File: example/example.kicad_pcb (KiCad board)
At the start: 2 copper layers, 43.2 x 35.6 mm, 12 parts, among them J1 Conn_01x07_Male, U1 LDC1314

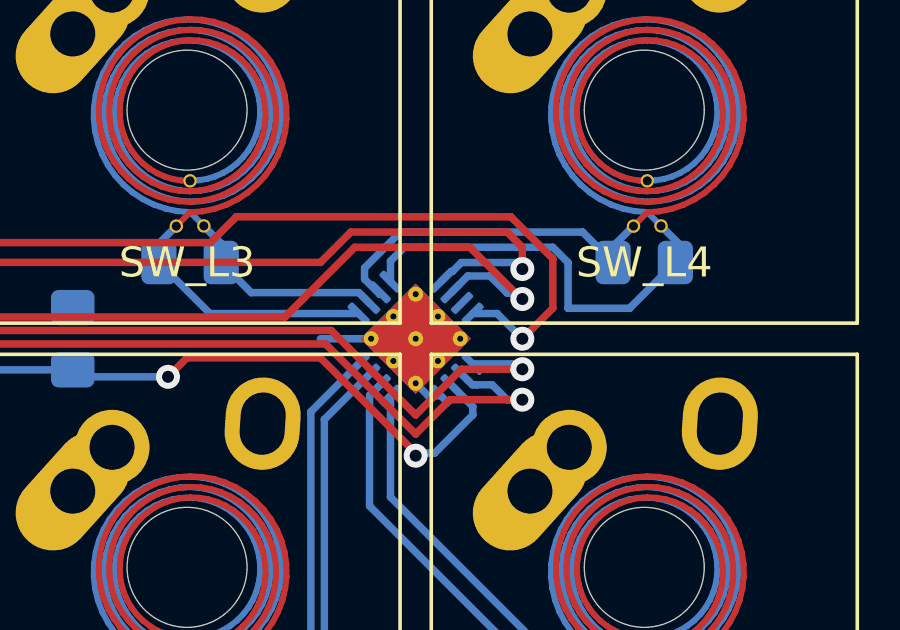
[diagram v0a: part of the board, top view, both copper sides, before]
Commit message: kikit for automatic fab output of example
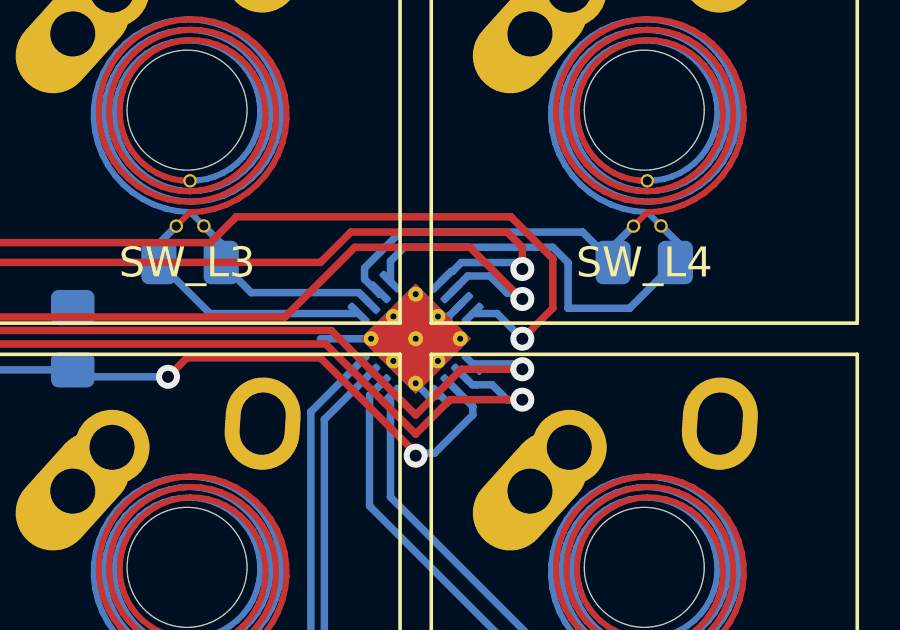
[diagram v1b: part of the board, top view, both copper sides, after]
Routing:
- net GND: track 2.70 -> 4.05 mm
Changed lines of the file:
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@@
   (segment (start 111.76 63.5) (end 111.76 65.024) (width 0.25) (layer "B.Cu") (net 8))
   (segment (start 105.840311 63.451407) (end 106.299718 62.992) (width 0.25) (layer "B.Cu") (net 8))
+  (segment (start 108.226796 64.846757) (end 107.776015 65.297538) (width 0.25) (layer "B.Cu") (net 9))
   (segment (start 107.095425 67.940349) (end 106.68 67.524924) (width 0.25) (layer "B.Cu") (net 9))
   (segment (start 105.195076 66.04) (end 103.505 66.04) (width 0.25) (layer "B.Cu") (net 9))
   (segment (start 107.519689 67.940349) (end 107.095425 67.940349) (width 0.25) (layer "B.Cu") (net 9))
+  (segment (start 107.776015 65.297538) (end 107.422462 65.297538) (width 0.25) (layer "B.Cu") (net 9))
+  (segment (start 107.776015 65.297538) (end 107.776015 65.651091) (width 0.25) (layer "B.Cu") (net 9))
   (segment (start 106.680101 69.851537) (end 103.504282 66.675718) (width 0.25) (layer "F.Cu") (net 10))
   (segment (start 103.504282 66.675718) (end 99.059282 66.675718) (width 0.25) (layer "F.Cu") (net 10))
